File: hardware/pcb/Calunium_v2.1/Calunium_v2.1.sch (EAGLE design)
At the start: 63 parts, among them IC1 MCP1702-3.3, IC2 DS1307, IC3 MCP1702-5.0, IC4 ATMEGA1284, IC5 MCP2200, Q1 2N7000, U1 CALUNIUM-SHIELD, X1 PWR, X2 JTAG, X3 USB, X4 CONN-SMATHD, X5 UART0, X6 MICRO-SD-SOCKETHIROSE-DM3D, Y1 32k768, Y2 16MHz, Y3 12MHz

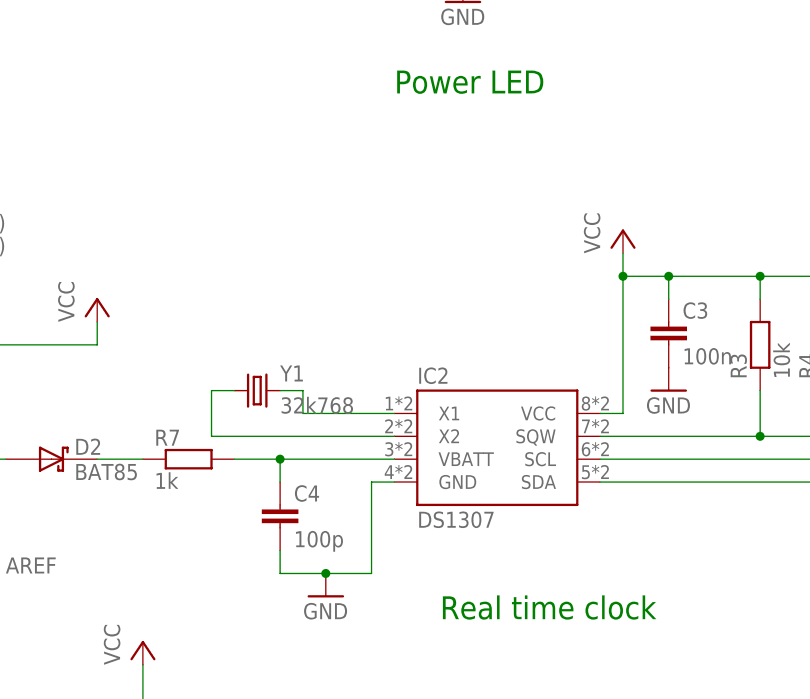
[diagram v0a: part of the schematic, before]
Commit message: Add load capacitors for MCP7941x RTC. Removed DIP footprint for RTC.
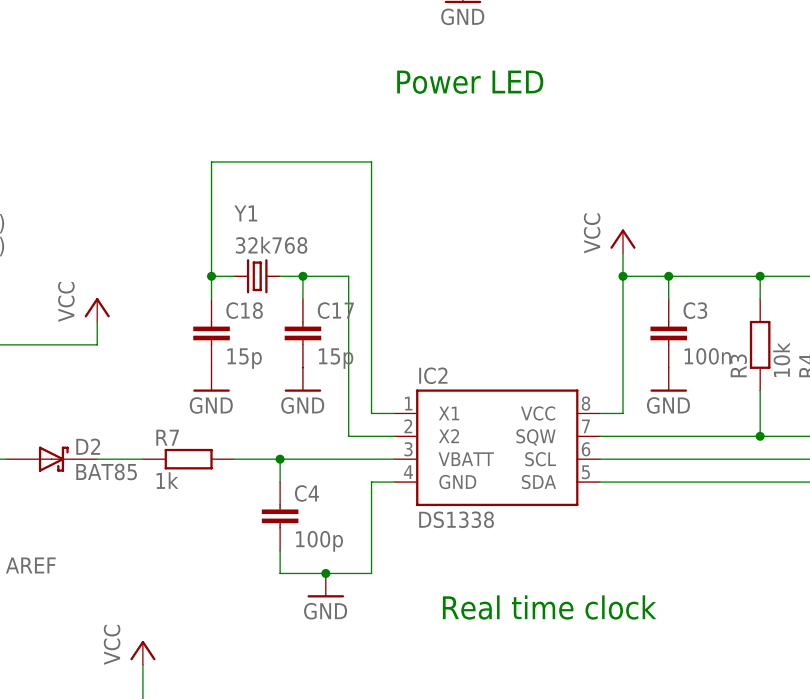
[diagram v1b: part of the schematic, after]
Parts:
- added C17, C18: 15p, SparkFun:CAPPTH
- IC2: value DS1307 -> DS1338; device SteveMarple:DS1307DIL08/SOIC8 -> SteveMarple:DS1307SO08
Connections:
- net GND: now also C17.2, C18.2
- net N$12: now also C17.1
- net N$5: now also C18.1
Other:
- moved on the sheet: Y1
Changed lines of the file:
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@@
 <grid distance="0.1" unitdist="inch" unit="inch" style="lines" multiple="1" display="no" altdistance="0.01" altunitdist="inch" altunit="inch"/>
 <layers>
-<layer number="1" name="Top" color="4" fill="1" visible="no" active="no"/>
-<layer number="2" name="Route2" color="1" fill="3" visible="no" active="no"/>
-<layer number="3" name="Route3" color="4" fill="3" visible="no" active="no"/>
-<layer number="14" name="Route14" color="1" fill="6" visible="no" active="no"/>
-<layer number="15" name="Route15" color="4" fill="6" visible="no" active="no"/>
-<layer number="16" name="Bottom" color="1" fill="1" visible="no" active="no"/>
-<layer number="17" name="Pads" color="2" fill="1" visible="no" active="no"/>
-<layer number="18" name="Vias" color="2" fill="1" visible="no" active="no"/>
-<layer number="19" name="Unrouted" color="6" fill="1" visible="no" active="no"/>
-<layer number="20" name="Dimension" color="15" fill="1" visible="no" active="no"/>
-<layer number="21" name="tPlace" color="7" fill="1" visible="no" active="no"/>
-<layer number="22" name="bPlace" color="7" fill="1" visible="no" active="no"/>
-<layer number="23" name="tOrigins" color="15" fill="1" visible="no" active="no"/>
-<layer number="24" name="bOrigins" color="15" fill="1" visible="no" active="no"/>
-<layer number="25" name="tNames" color="7" fill="1" visible="no" active="no"/>
-<layer number="26" name="bNames" color="7" fill="1" visible="no" active="no"/>
-<layer number="27" name="tValues" color="7" fill="1" visible="no" active="no"/>
-<layer number="28" name="bValues" color="7" fill="1" visible="no" active="no"/>
+<layer number="1" name="Top" color="4" fill="1" visible="yes" active="no"/>
+<layer number="2" name="Route2" color="1" fill="3" visible="yes" active="no"/>
+<layer number="3" name="Route3" color="4" fill="3" visible="yes" active="no"/>
+<layer number="14" name="Route14" color="1" fill="6" visible="yes" active="no"/>
+<layer number="15" name="Route15" color="4" fill="6" visible="yes" active="no"/>
+<layer number="16" name="Bottom" color="1" fill="1" visible="yes" active="no"/>
+<layer number="17" name="Pads" color="2" fill="1" visible="yes" active="no"/>
+<layer number="18" name="Vias" color="2" fill="1" visible="yes" active="no"/>
+<layer number="19" name="Unrouted" color="6" fill="1" visible="yes" active="no"/>
+<layer number="20" name="Dimension" color="15" fill="1" visible="yes" active="no"/>
+<layer number="21" name="tPlace" color="7" fill="1" visible="yes" active="no"/>
+<layer number="22" name="bPlace" color="7" fill="1" visible="yes" active="no"/>
+<layer number="23" name="tOrigins" color="15" fill="1" visible="yes" active="no"/>
+<layer number="24" name="bOrigins" color="15" fill="1" visible="yes" active="no"/>
+<layer number="25" name="tNames" color="7" fill="1" visible="yes" active="no"/>
+<layer number="26" name="bNames" color="7" fill="1" visible="yes" active="no"/>
+<layer number="27" name="tValues" color="7" fill="1" visible="yes" active="no"/>
+<layer number="28" name="bValues" color="7" fill="1" visible="yes" active="no"/>
 <layer number="29" name="tStop" color="7" fill="3" visible="no" active="no"/>
 <layer number="30" name="bStop" color="7" fill="6" visible="no" active="no"/>
@@
 <layer number="35" name="tGlue" color="7" fill="4" visible="no" active="no"/>
 <layer number="36" name="bGlue" color="7" fill="5" visible="no" active="no"/>
-<layer number="37" name="tTest" color="7" fill="1" visible="no" active="no"/>
-<layer number="38" name="bTest" color="7" fill="1" visible="no" active="no"/>
+<layer number="37" name="tTest" color="7" fill="1" visible="yes" active="no"/>
+<layer number="38" name="bTest" color="7" fill="1" visible="yes" active="no"/>
 <layer number="39" name="tKeepout" color="4" fill="11" visible="no" active="no"/>
 <layer number="40" name="bKeepout" color="1" fill="11" visible="no" active="no"/>
@@
 <layer number="44" name="Drills" color="7" fill="1" visible="no" active="no"/>
 <layer number="45" name="Holes" color="7" fill="1" visible="no" active="no"/>
-<layer number="46" name="Milling" color="3" fill="1" visible="no" active="no"/>
-<layer number="47" name="Measures" color="7" fill="1" visible="no" active="no"/>
-<layer number="48" name="Document" color="7" fill="1" visible="no" active="no"/>
-<layer number="49" name="Reference" color="7" fill="1" visible="no" active="no"/>
-<layer number="50" name="dxf" color="7" fill="1" visible="no" active="no"/>
-<layer number="51" name="tDocu" color="7" fill="1" visible="no" active="no"/>
-<layer number="52" name="bDocu" color="7" fill="1" visible="no" active="no"/>
-<layer number="53" name="tGND_GNDA" color="7" fill="9" visible="no" active="no"/>
-<layer number="54" name="bGND_GNDA" color="1" fill="9" visible="no" active="no"/>
-<layer number="56" name="wert" color="7" fill="1" visible="no" active="no"/>
+<layer number="46" name="Milling" color="3" fill="1" visible="yes" active="no"/>
+<layer number="47" name="Measures" color="7" fill="1" visible="yes" active="no"/>
+<layer number="48" name="Document" color="7" fill="1" visible="yes" active="no"/>
+<layer number="49" name="Reference" color="7" fill="1" visible="yes" active="no"/>
+<layer number="50" name="dxf" color="7" fill="1" visible="yes" active="no"/>
+<layer number="51" name="tDocu" color="7" fill="1" visible="yes" active="no"/>
+<layer number="52" name="bDocu" color="7" fill="1" visible="yes" active="no"/>
+<layer number="53" name="tGND_GNDA" color="7" fill="9" visible="yes" active="no"/>
+<layer number="54" name="bGND_GNDA" color="1" fill="9" visible="yes" active="no"/>
+<layer number="56" name="wert" color="7" fill="1" visible="yes" active="no"/>
 <layer number="91" name="Nets" color="2" fill="1" visible="yes" active="yes"/>
 <layer number="92" name="Busses" color="1" fill="1" visible="yes" active="yes"/>
@@
 <part name="Q1" library="SteveMarple" deviceset="2N7000" device=""/>
 <part name="U1" library="SteveMarple" deviceset="CALUNIUM-SHIELD-V2" device="NO-OUTLINE-NO-HOLES-NO-TEXT" value="CALUNIUM-SHIELD"/>
-<part name="IC2" library="SteveMarple" deviceset="DS1307" device="DIL08/SOIC8" value="DS1307"/>
+<part name="IC2" library="SteveMarple" deviceset="DS1307" device="SO08" value="DS1338"/>
 <part name="LED1" library="SparkFun" deviceset="LED" device="3MM" value="D13"/>
 <part name="LED2" library="SparkFun" deviceset="LED" device="3MM" value="PWR"/>
@@
 <part name="GND23" library="supply1" deviceset="GND" device=""/>
 <part name="GND24" library="supply1" deviceset="GND" device=""/>
+<part name="C17" library="SparkFun" deviceset="CAP" device="PTH" value="15p"/>
+<part name="C18" library="SparkFun" deviceset="CAP" device="PTH" value="15p"/>
+<part name="GND29" library="supply1" deviceset="GND" device=""/>
+<part name="GND30" library="supply1" deviceset="GND" device=""/>
 </parts>
 <sheets>
@@
 <instance part="LED2" gate="G$1" x="137.16" y="124.46"/>
 <instance part="R1" gate="G$1" x="185.42" y="142.24" rot="R90"/>
-<instance part="Y1" gate="G$1" x="114.3" y="73.66"/>
+<instance part="Y1" gate="G$1" x="114.3" y="86.36" smashed="yes" rot="R180">
+<attribute name="NAME" x="111.76" y="92.456" size="1.778" layer="95"/>
+<attribute name="VALUE" x="111.76" y="88.9" size="1.778" layer="96"/>
+</instance>
 <instance part="R2" gate="G$1" x="137.16" y="132.08" rot="R90"/>
 <instance part="JP2" gate="G$1" x="-7.62" y="154.94"/>
@@
 <instance part="GND23" gate="1" x="-12.7" y="-58.42"/>
 <instance part="GND24" gate="1" x="10.16" y="-58.42"/>
+<instance part="C17" gate="G$1" x="119.38" y="78.74"/>
+<instance part="C18" gate="G$1" x="109.22" y="78.74"/>
+<instance part="GND29" gate="1" x="119.38" y="73.66"/>
+<instance part="GND30" gate="1" x="109.22" y="73.66"/>
 </instances>
 <busses>
@@
 <pinref part="C16" gate="G$1" pin="2"/>
 <wire x1="10.16" y1="-55.88" x2="10.16" y2="-53.34" width="0.1524" layer="91"/>
+</segment>
+<segment>
+<pinref part="C17" gate="G$1" pin="2"/>
+<pinref part="GND29" gate="1" pin="GND"/>
+</segment>
+<segment>
+<pinref part="C18" gate="G$1" pin="2"/>
+<pinref part="GND30" gate="1" pin="GND"/>
 </segment>
 </net>
@@
 <net name="N$5" class="0">
 <segment>
-<wire x1="119.38" y1="71.12" x2="129.54" y2="71.12" width="0.1524" layer="91"/>
-<wire x1="119.38" y1="73.66" x2="119.38" y2="71.12" width="0.1524" layer="91"/>
-<wire x1="116.84" y1="73.66" x2="119.38" y2="73.66" width="0.1524" layer="91"/>
+<wire x1="127" y1="71.12" x2="129.54" y2="71.12" width="0.1524" layer="91"/>
+<wire x1="127" y1="99.06" x2="127" y2="71.12" width="0.1524" layer="91"/>
+<wire x1="109.22" y1="83.82" x2="109.22" y2="86.36" width="0.1524" layer="91"/>
+<wire x1="109.22" y1="86.36" x2="109.22" y2="99.06" width="0.1524" layer="91"/>
+<wire x1="109.22" y1="99.06" x2="127" y2="99.06" width="0.1524" layer="91"/>
 <pinref part="IC2" gate="G$1" pin="X1"/>
 <pinref part="Y1" gate="G$1" pin="2"/>
+<pinref part="C18" gate="G$1" pin="1"/>
+<junction x="109.22" y="86.36"/>
+<wire x1="109.22" y1="86.36" x2="111.76" y2="86.36" width="0.1524" layer="91"/>
 </segment>
 </net>
@@
 <net name="N$12" class="0">
 <segment>
-<wire x1="111.76" y1="73.66" x2="109.22" y2="73.66" width="0.1524" layer="91"/>
-<wire x1="109.22" y1="73.66" x2="109.22" y2="68.58" width="0.1524" layer="91"/>
-<wire x1="129.54" y1="68.58" x2="109.22" y2="68.58" width="0.1524" layer="91"/>
+<wire x1="116.84" y1="86.36" x2="119.38" y2="86.36" width="0.1524" layer="91"/>
+<wire x1="119.38" y1="86.36" x2="119.38" y2="83.82" width="0.1524" layer="91"/>
+<wire x1="124.46" y1="86.36" x2="124.46" y2="68.58" width="0.1524" layer="91"/>
+<wire x1="129.54" y1="68.58" x2="124.46" y2="68.58" width="0.1524" layer="91"/>
 <pinref part="Y1" gate="G$1" pin="1"/>
 <pinref part="IC2" gate="G$1" pin="X2"/>
-</segment>
-</net>
+<pinref part="C17" gate="G$1" pin="1"/>
+<junction x="119.38" y="86.36"/>
+<wire x1="119.38" y1="86.36" x2="124.46" y2="86.36" width="0.1524" layer="91"/>
+</segment>
+</net>
